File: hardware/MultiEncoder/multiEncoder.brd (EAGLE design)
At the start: 100 x 80 mm, 23 parts, among them J1 90325-0004, J2 90325-0004, J3 90325-0004, J4 90325-0004, J5 90325-0004, J6 90325-0004, U1 MCP23017-E/SP

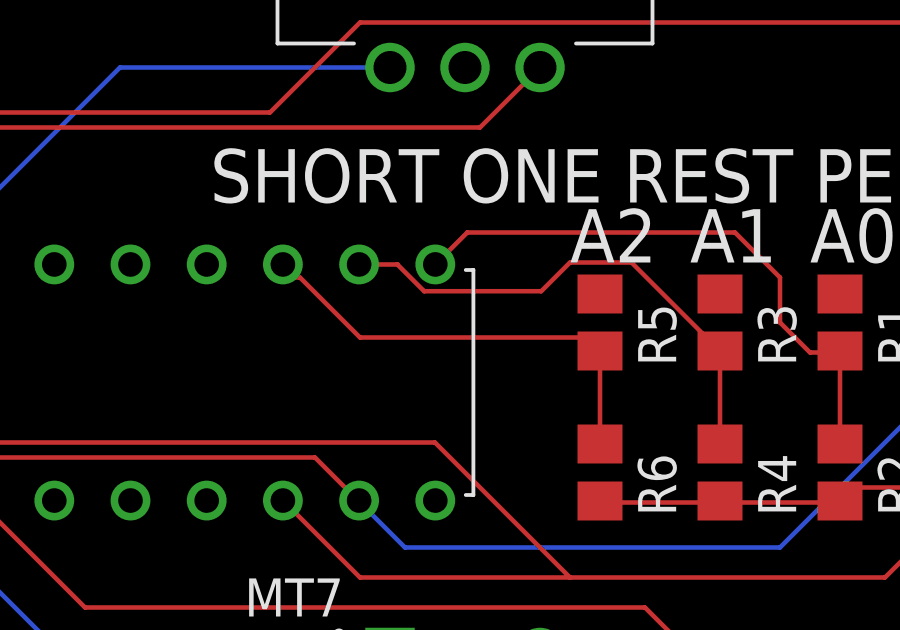
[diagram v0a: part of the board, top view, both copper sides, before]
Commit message: move addr1 line away from addr0 pad, regenerate gerbers
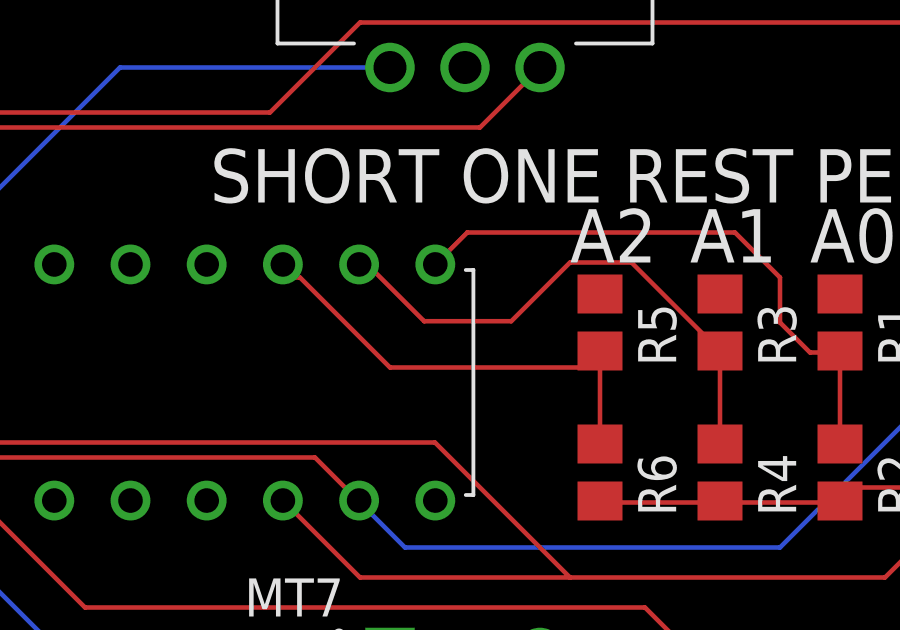
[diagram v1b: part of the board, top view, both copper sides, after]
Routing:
- net ADR1: track 17.1 -> 17.9 mm
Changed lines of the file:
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@@
 <contactref element="U1" pad="17"/>
 <wire x1="67" y1="41.05" x2="67" y2="37.95" width="0.1524" layer="1"/>
-<wire x1="59" y1="41.5" x2="67" y2="41.5" width="0.1524" layer="1"/>
-<wire x1="57" y1="43.5" x2="59" y2="41.5" width="0.1524" layer="1"/>
+<wire x1="67" y1="41.05" x2="66.45" y2="40.5" width="0.1524" layer="1"/>
+<wire x1="66.45" y1="40.5" x2="60" y2="40.5" width="0.1524" layer="1"/>
+<wire x1="57" y1="43.5" x2="60" y2="40.5" width="0.1524" layer="1"/>
 <wire x1="56.5" y1="43.5" x2="57" y2="43.5" width="0.1524" layer="1"/>
-<wire x1="67" y1="41.5" x2="67" y2="41.05" width="0.1524" layer="1"/>
 <wire x1="56.5" y1="43.5" x2="56.43" y2="43.935" width="0.1524" layer="1"/>
 </signal>
@@
 <contactref element="R4" pad="1"/>
 <contactref element="U1" pad="16"/>
-<wire x1="58.97" y1="43.935" x2="60.24766875" y2="43.935" width="0.1524" layer="1"/>
-<wire x1="60.24766875" y1="43.935" x2="61.14026875" y2="43.0424" width="0.1524" layer="1"/>
-<wire x1="61.14026875" y1="43.0424" x2="65.0424" y2="43.0424" width="0.1524" layer="1"/>
-<wire x1="65.0424" y1="43.0424" x2="66" y2="44" width="0.1524" layer="1"/>
+<wire x1="58.97" y1="43.935" x2="59.24766875" y2="43.935" width="0.1524" layer="1"/>
+<wire x1="59.24766875" y1="43.935" x2="61.14026875" y2="42.0424" width="0.1524" layer="1"/>
+<wire x1="61.14026875" y1="42.0424" x2="64.0424" y2="42.0424" width="0.1524" layer="1"/>
+<wire x1="64.0424" y1="42.0424" x2="66" y2="44" width="0.1524" layer="1"/>
 <wire x1="68.05" y1="44" x2="71" y2="41.05" width="0.1524" layer="1"/>
 <wire x1="66" y1="44" x2="68.05" y2="44" width="0.1524" layer="1"/>
